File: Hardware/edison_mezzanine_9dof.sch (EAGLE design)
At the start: 42 parts, among them U1 LSM9DS0, U2 EDISON_CONNECTOR_FULLMOUNTING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, U3 EDISON_CONNECTOR_FULLHEADER, U4 MIC52053.3V

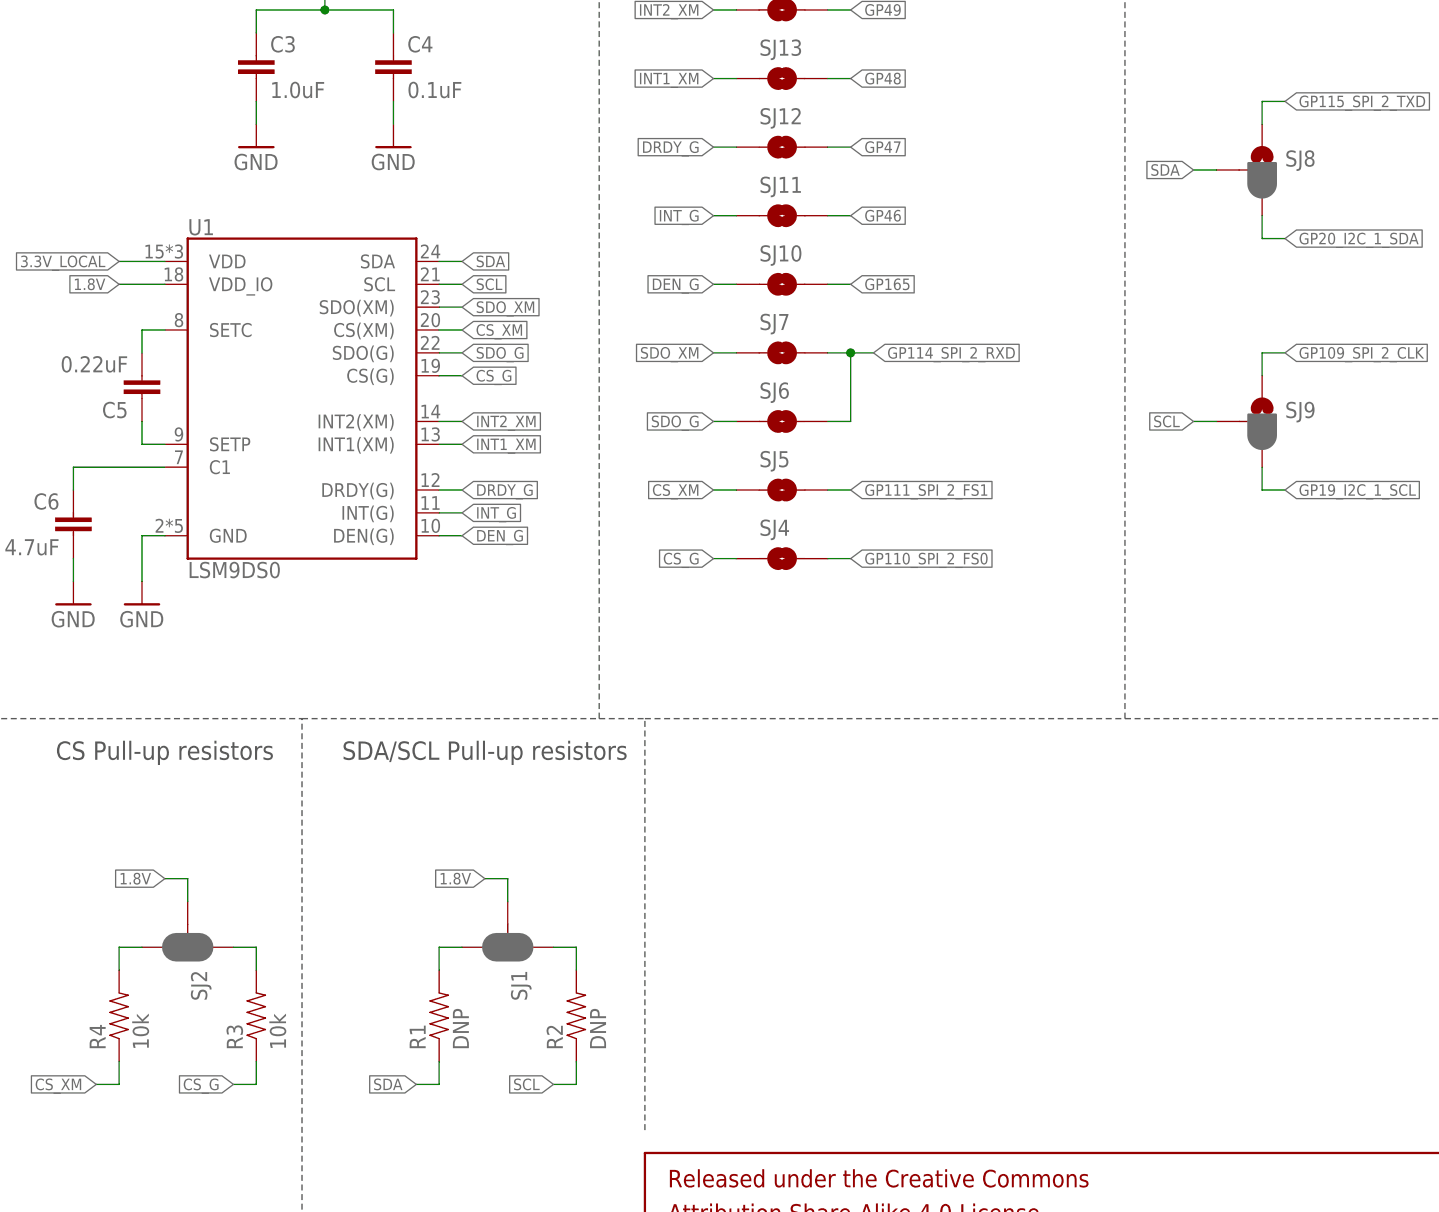
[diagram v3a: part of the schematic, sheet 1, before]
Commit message: Paste to trace jumpers, edit packages
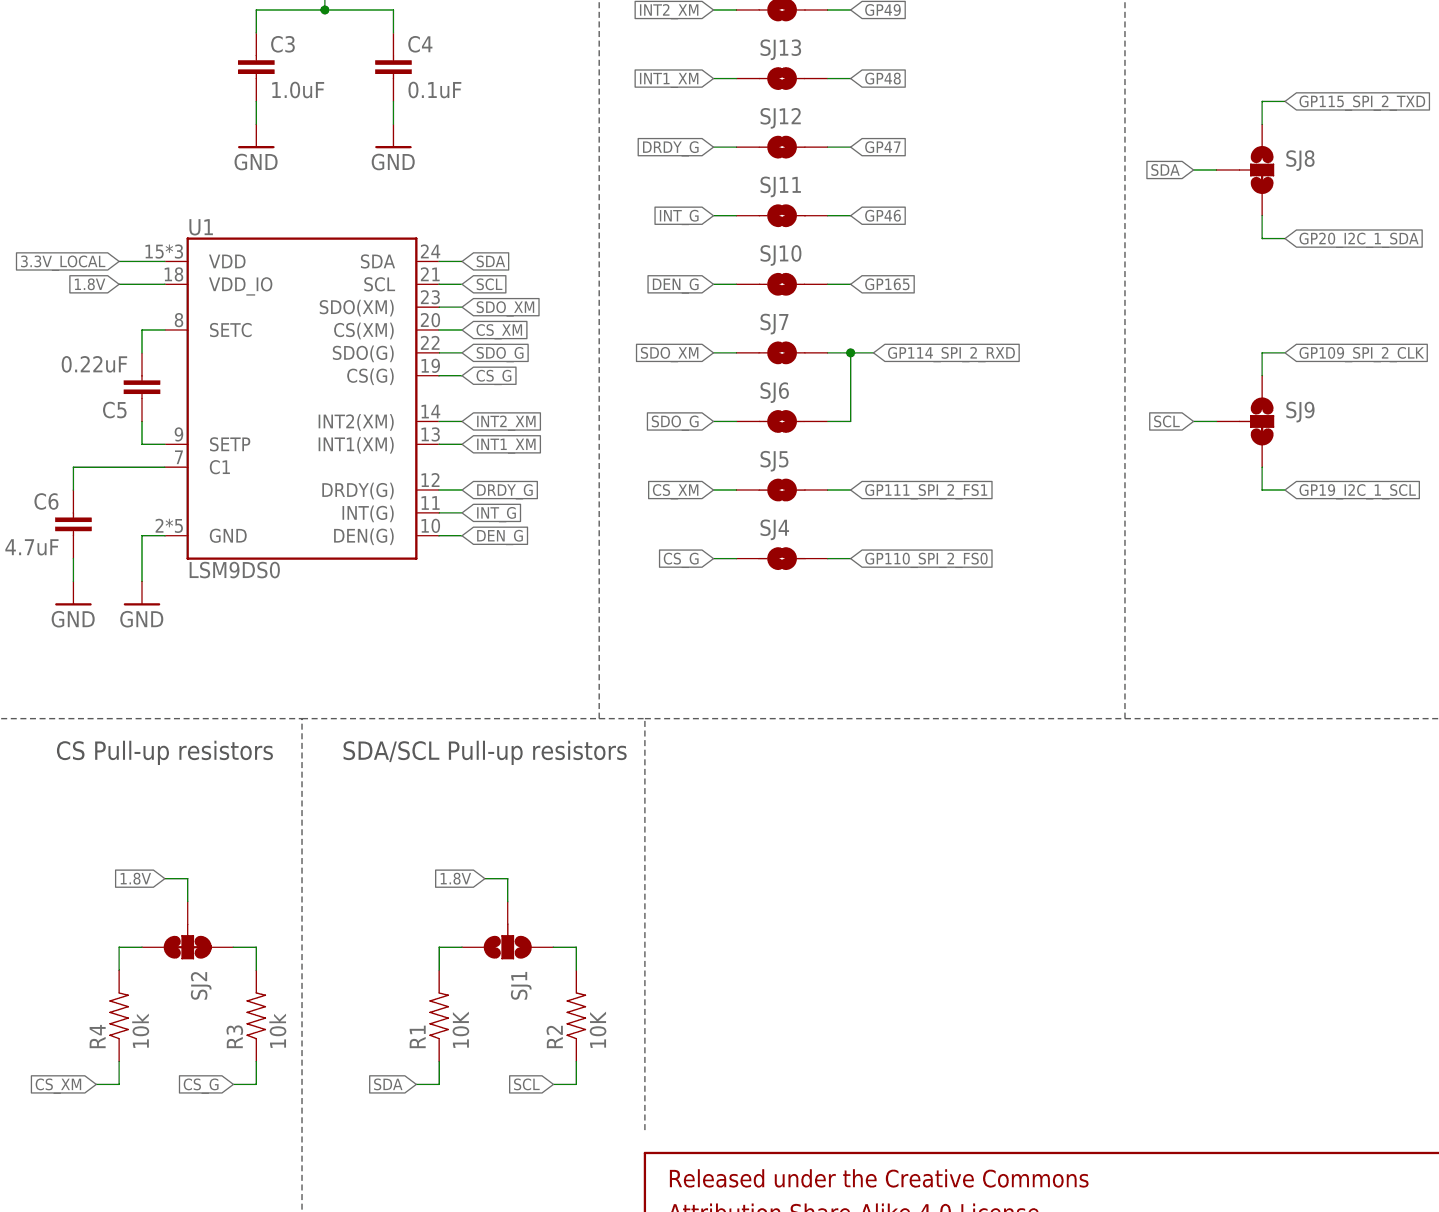
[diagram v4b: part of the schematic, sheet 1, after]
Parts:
- R1, R2: value DNP -> 10K; device SparkFun-Resistors:10K-1%RES-00824 -> SparkFun-Resistors:10KOHM1/10W1%(0603)0603
- SJ1: value JUMPER-PAD-3-NC_BY_PASTE -> JUMPER-PAD-3-NOYES_SILK; device SparkFun-Passives:JUMPER-PAD-3-NC_BY_PASTE -> SparkFun-Passives:JUMPER-PAD-3-NOYES_SILK
- SJ2: value JUMPER-PAD-3-NC_BY_PASTE -> (none); device SparkFun-Passives:JUMPER-PAD-3-NC_BY_PASTE -> SparkFun-Passives:JUMPER-PAD-3-NC_BY_TRACE
- SJ8, SJ9: value JUMPER-PAD-3-2OF3_NC_BY_PASTE -> JUMPER-PAD-3-2OF3_NC_BY_TRACE_SMALL; device SparkFun-Passives:JUMPER-PAD-3-2OF3_NC_BY_PASTE -> SparkFun-Passives:JUMPER-PAD-3-2OF3_NC_BY_TRACE_SMALL
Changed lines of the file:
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@@
 <part name="C3" library="SparkFun-Capacitors" deviceset="1.0UF-16V-10%(0603)" device="" value="1.0uF"/>
 <part name="GND5" library="SparkFun-Aesthetics" deviceset="GND" device=""/>
-<part name="R1" library="SparkFun-Resistors" deviceset="10K-1%" device="RES-00824" value="DNP"/>
-<part name="R2" library="SparkFun-Resistors" deviceset="10K-1%" device="RES-00824" value="DNP"/>
+<part name="R1" library="SparkFun-Resistors" deviceset="10KOHM1/10W1%(0603)" device="0603" value="10K"/>
+<part name="R2" library="SparkFun-Resistors" deviceset="10KOHM1/10W1%(0603)" device="0603" value="10K"/>
 <part name="R3" library="SparkFun-Resistors" deviceset="10K-1%" device="RES-00824" value="10k"/>
 <part name="R4" library="SparkFun-Resistors" deviceset="10K-1%" device="RES-00824" value="10k"/>
@@
 <part name="SJ13" library="SparkFun-Passives" deviceset="JUMPER-PAD-2-NO" device="YES_SILK"/>
 <part name="SJ14" library="SparkFun-Passives" deviceset="JUMPER-PAD-2-NO" device="YES_SILK"/>
-<part name="SJ8" library="SparkFun-Passives" deviceset="JUMPER-PAD-3-2OF3_NC_BY_PASTE" device=""/>
-<part name="SJ9" library="SparkFun-Passives" deviceset="JUMPER-PAD-3-2OF3_NC_BY_PASTE" device=""/>
+<part name="SJ8" library="SparkFun-Passives" deviceset="JUMPER-PAD-3-2OF3_NC_BY_TRACE" device="_SMALL"/>
+<part name="SJ9" library="SparkFun-Passives" deviceset="JUMPER-PAD-3-2OF3_NC_BY_TRACE" device="_SMALL"/>
 <part name="GND7" library="SparkFun-Aesthetics" deviceset="GND" device=""/>
-<part name="SJ2" library="SparkFun-Passives" deviceset="JUMPER-PAD-3-NC_BY_PASTE" device=""/>
-<part name="SJ1" library="SparkFun-Passives" deviceset="JUMPER-PAD-3-NC_BY_PASTE" device=""/>
+<part name="SJ2" library="SparkFun-Passives" deviceset="JUMPER-PAD-3-NC_BY_TRACE" device=""/>
+<part name="SJ1" library="SparkFun-Passives" deviceset="JUMPER-PAD-3-NO" device="YES_SILK"/>
 <part name="U4" library="SparkFun-PowerIC" deviceset="MIC5205" device="3.3V" value="MIC52053.3V"/>
 <part name="C1" library="SparkFun-Capacitors" deviceset="1.0UF-16V-10%(0603)" device="" value="1.0uF"/>
